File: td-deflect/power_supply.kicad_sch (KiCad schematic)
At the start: 94 parts, among them J13 Conn_01x02_Male, J14 Conn_01x02_Male, J18 Conn_01x02_Male, J2 Conn_01x02_Male, J9 Conn_01x02_Male, Q12 G3R450MT17J, Q13 BSZ42DN25NS3GATMA1, U13 MCP1416, U14 LT3758AEMSE

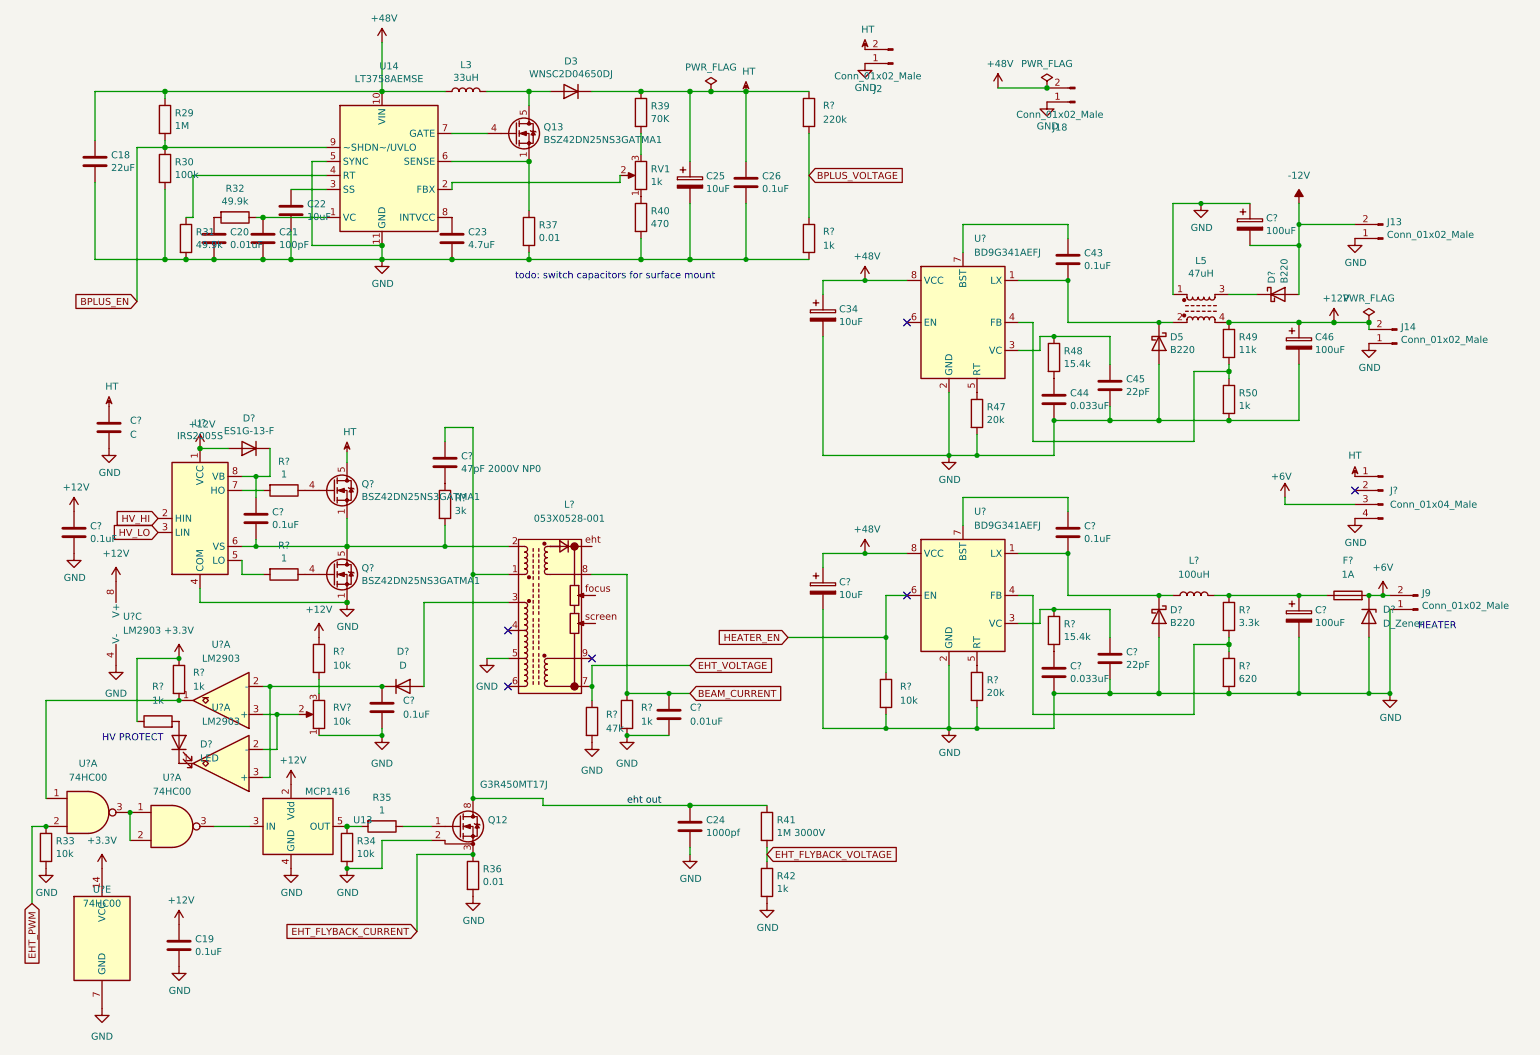
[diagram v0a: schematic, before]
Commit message: update kicad format and move flyback to separate sheet
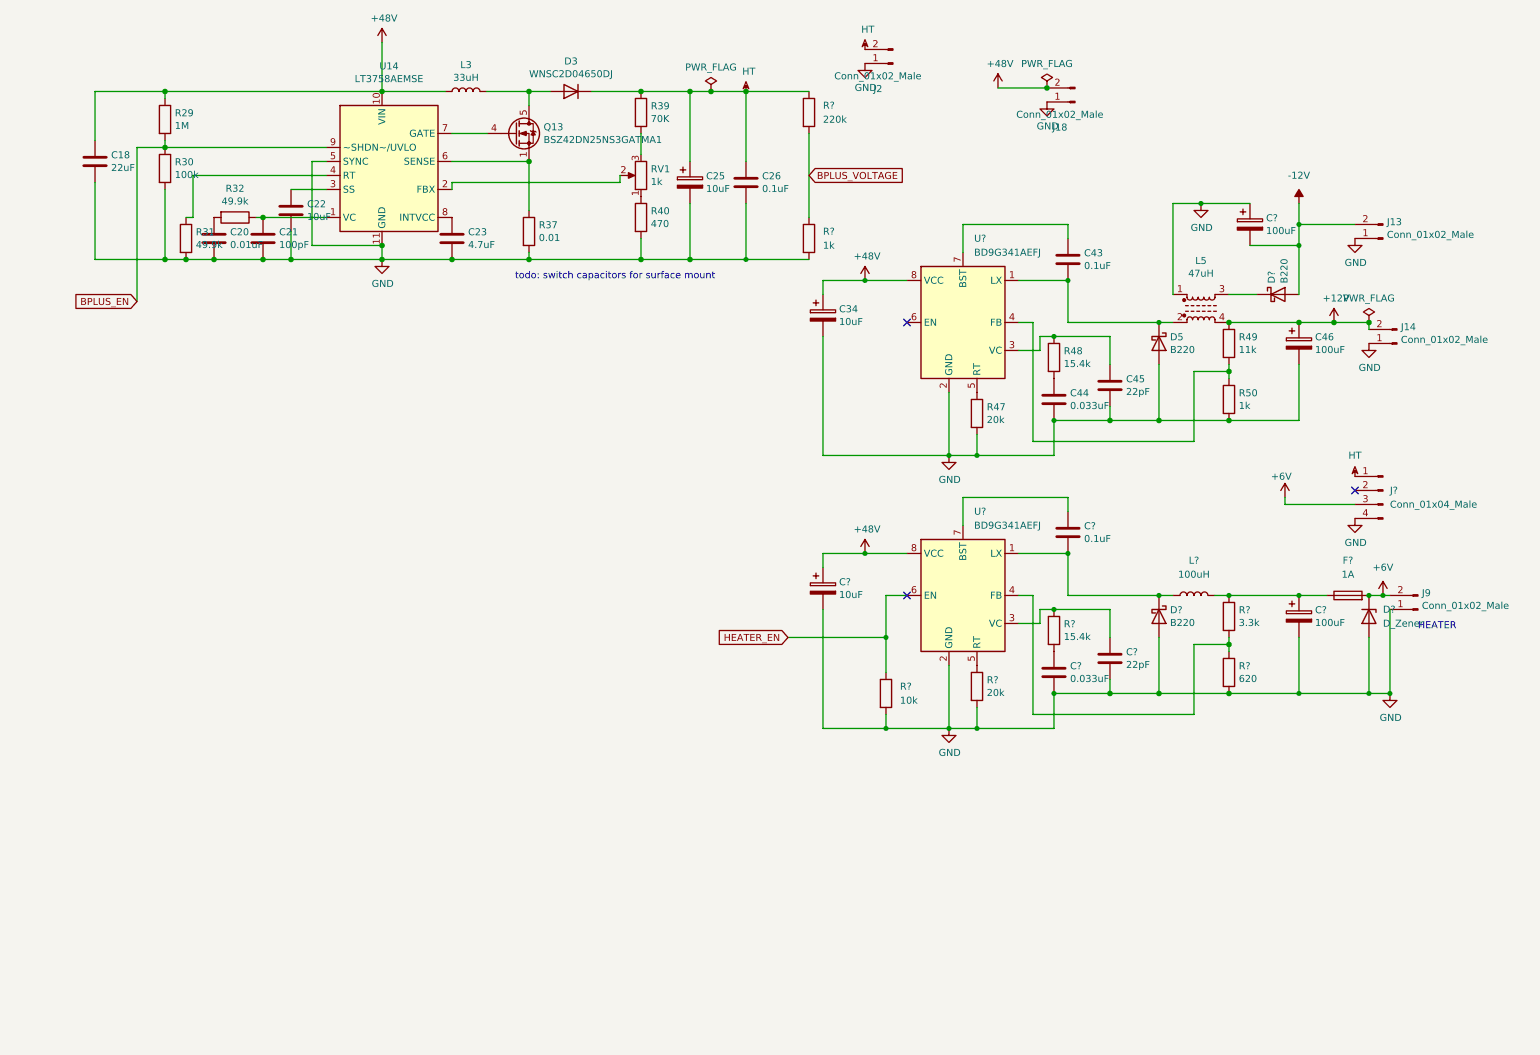
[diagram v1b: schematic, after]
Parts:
- removed C19, C? (x2): 0.1uF, Capacitor_SMD:C_0805_2012Metric_Pad1.15x1.40mm_HandSolder, symbol Device:C
- removed C24: 1000pf, Capacitor_THT:C_Rect_L18.0mm_W6.0mm_P15.00mm_FKS3_FKP3, symbol Device:C
- removed C?: C, symbol Device:C
- removed C?: 0.1uF, symbol Device:C
- removed C?: 47pF 2000V NP0, Capacitor_SMD:C_1206_3216Metric, symbol Device:C
- removed C?: 0.01uF, symbol Device:C
- removed D?: D, symbol Device:D
- removed D?: LED, symbol Device:LED
- removed D?: ES1G-13-F, Diode_SMD:D_SMA, symbol Diode:BA157
- removed L?: 053X0528-001, symbol td-hv:053X0528-001
- removed Q12: G3R450MT17J, Package_TO_SOT_SMD:TO-263-7_TabPin8, symbol Transistor_FET:C3M0280090J
- removed Q? (x2): BSZ42DN25NS3GATMA1, Package_TO_SOT_SMD:TDSON-8-1, symbol Transistor_FET:BSC082N10LSG
- removed R33, R34: 10k, Resistor_SMD:R_0805_2012Metric_Pad1.15x1.40mm_HandSolder, symbol Device:R
- removed R35, R? (x2): 1, Resistor_SMD:R_0805_2012Metric_Pad1.15x1.40mm_HandSolder, symbol Device:R
- removed R36: 0.01, Resistor_SMD:R_0805_2012Metric_Pad1.15x1.40mm_HandSolder, symbol Device:R
- removed R41: 1M 3000V, Resistor_SMD:R_2512_6332Metric, symbol Device:R
- removed R42: 1k, Resistor_SMD:R_0805_2012Metric_Pad1.15x1.40mm_HandSolder, symbol Device:R
- removed R? (x3): 1k, symbol Device:R
- removed R?: 3k, Resistor_SMD:R_2512_6332Metric, symbol Device:R
- removed R?: 10k, symbol Device:R
- removed R?: 47k, symbol Device:R
- removed RV?: 10k, symbol Device:R_Potentiometer
- removed U13: MCP1416, Package_TO_SOT_SMD:SOT-23-5, symbol Driver_FET:MCP1416
- removed U? (x3): 74HC00, symbol 74xx:74HC00
- removed U?: IRS2005S, Package_SO:SOIC-8_3.9x4.9mm_P1.27mm, symbol Driver_FET:IRS2005S
- removed U? (x3): LM2903, symbol Comparator:LM2903
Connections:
- no-connect marks 6 -> 3
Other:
- note removed: "HV PROTECT"

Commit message: Add independent cathode supply
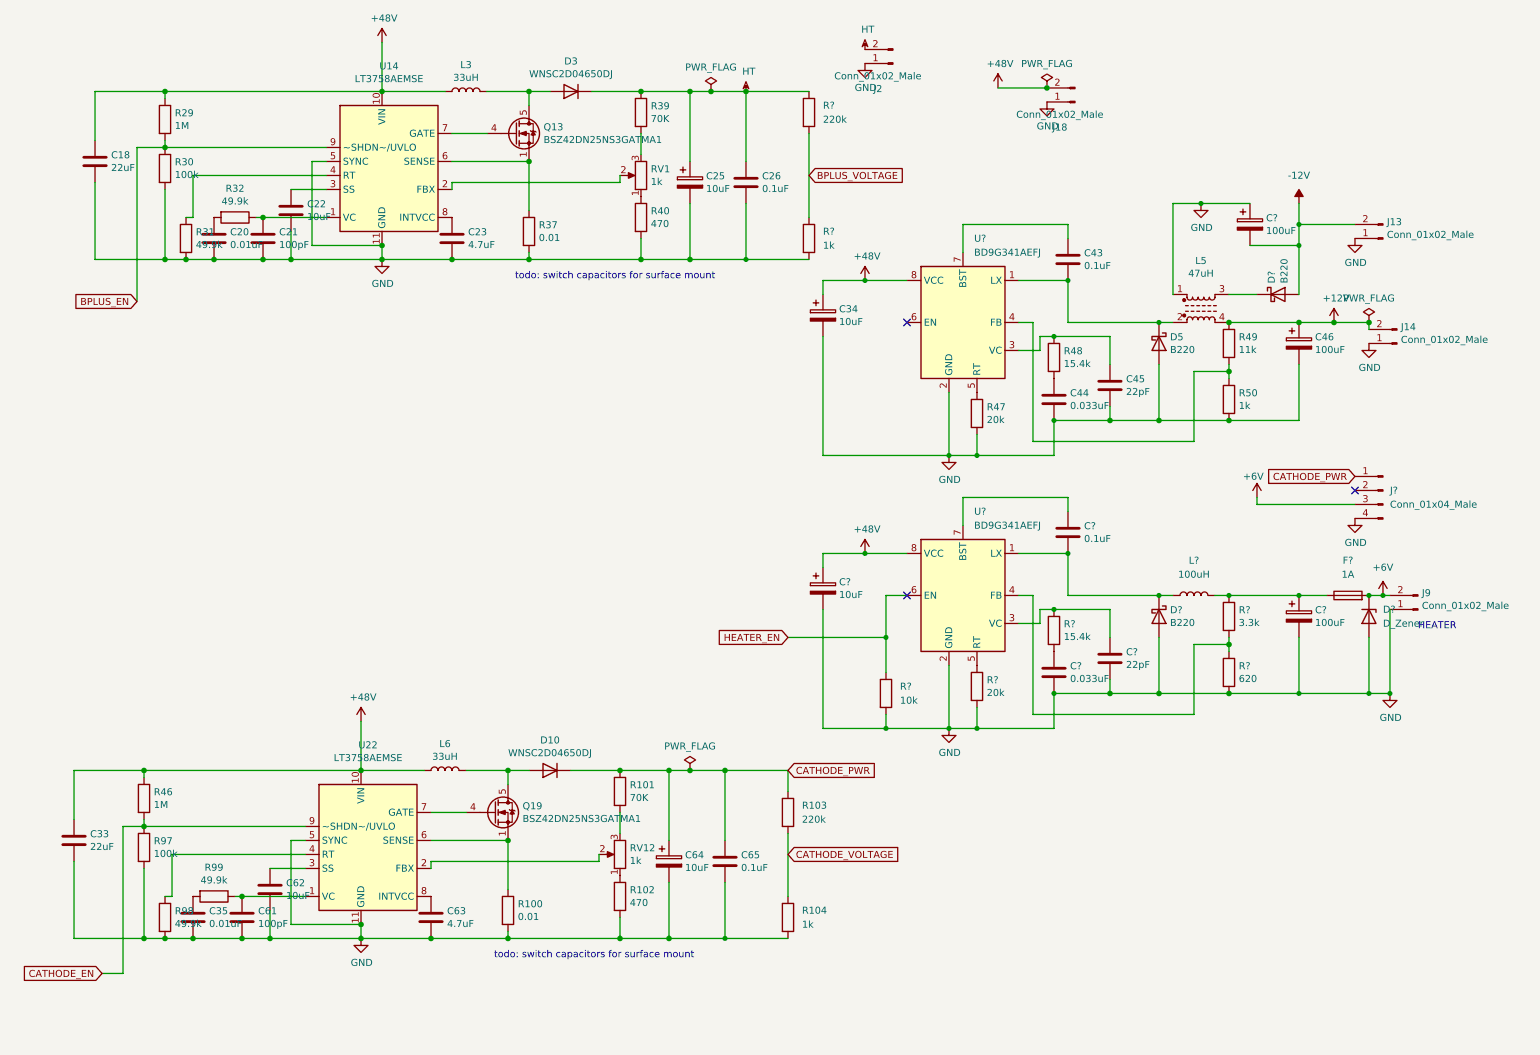
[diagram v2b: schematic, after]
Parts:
- added C33: 22uF, Capacitor_THT:CP_Radial_D8.0mm_P3.50mm, symbol Device:C
- added C35: 0.01uF, Capacitor_SMD:C_0805_2012Metric_Pad1.15x1.40mm_HandSolder, symbol Device:C
- added C61: 100pF, Capacitor_SMD:C_0805_2012Metric_Pad1.15x1.40mm_HandSolder, symbol Device:C
- added C62: 10uF, Capacitor_SMD:C_1206_3216Metric_Pad1.42x1.75mm_HandSolder, symbol Device:C
- added C63: 4.7uF, Capacitor_SMD:C_0805_2012Metric_Pad1.15x1.40mm_HandSolder, symbol Device:C
- added C64: 10uF, Capacitor_THT:CP_Radial_D8.0mm_P3.50mm, symbol Device:CP
- added C65: 0.1uF, Capacitor_SMD:C_1206_3216Metric_Pad1.42x1.75mm_HandSolder, symbol Device:C
- added D10: WNSC2D04650DJ, Package_TO_SOT_SMD:TO-252-2_TabPin1, symbol Diode:1N5402
- added L6: 33uH, Inductor_SMD:L_Bourns_SRR1260, symbol Device:L
- added Q19: BSZ42DN25NS3GATMA1, Package_TO_SOT_SMD:TDSON-8-1, symbol Transistor_FET:BSC082N10LSG
- added R100: 0.01, Resistor_SMD:R_0805_2012Metric_Pad1.15x1.40mm_HandSolder, symbol Device:R
- added R101: 70K, Resistor_SMD:R_1206_3216Metric_Pad1.42x1.75mm_HandSolder, symbol Device:R
- added R102: 470, Resistor_SMD:R_0805_2012Metric_Pad1.15x1.40mm_HandSolder, symbol Device:R
- added R103: 220k, symbol Device:R
- added R104: 1k, symbol Device:R
- added R46: 1M, Resistor_SMD:R_0805_2012Metric_Pad1.15x1.40mm_HandSolder, symbol Device:R
- added R97: 100k, Resistor_SMD:R_0805_2012Metric_Pad1.15x1.40mm_HandSolder, symbol Device:R
- added R98, R99: 49.9k, Resistor_SMD:R_0805_2012Metric_Pad1.15x1.40mm_HandSolder, symbol Device:R
- added RV12: 1k, Potentiometer_THT:Potentiometer_Bourns_3386P_Vertical, symbol Device:R_POT
- added U22: LT3758AEMSE, Package_SO:MSOP-10-1EP_3x3mm_P0.5mm_EP1.68x1.88mm, symbol Regulator_Switching:LT3757AEMSE
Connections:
- net +48V: now also C33.1, L6.1, R46.1, U22.10 (VIN)
- net GND: now also C33.2, C35.2, C61.2, C62.2, C63.2, C64.2, C65.2, R100.2, R102.2, R104.2, R97.2, R98.2, U22.11 (GND), U22.5 (SYNC)
- net HT: no longer J?.1 (Pin_1)
- new net: C61.1, R99.1, U22.1 (VC)
- new net: RV12.2, U22.2 (FBX)
- new net: C62.1, U22.3 (SS)
- new net: R98.1, U22.4 (RT)
- new net: Q19.1 (S), Q19.2 (S), Q19.3 (S), R100.1, U22.6 (SENSE)
- new net: Q19.4 (G), U22.7 (GATE)
- new net: C63.1, U22.8 (INTVCC)
- new net: C35.1, R99.2
- new net: R102.1, RV12.1
- new net: R101.2, RV12.3
- new net: D10.2 (A), L6.2, Q19.5 (D)
- new net CATHODE_EN: R46.2, R97.1, U22.9 (~SHDN~/UVLO)
- new net CATHODE_PWR: C64.1, C65.1, D10.1 (K), J?.1 (Pin_1), R101.1, R103.1
- new net CATHODE_VOLTAGE: R103.2, R104.1

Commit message: more updates
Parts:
- R103, R104: footprint (none) -> Resistor_SMD:R_0805_2012Metric_Pad1.15x1.40mm_HandSolder
- R73, R74, R75: renamed from R?; footprint (none) -> Resistor_SMD:R_0805_2012Metric_Pad1.15x1.40mm_HandSolder
- gave numbers to parts that had none: 18

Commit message: even more updates
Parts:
- F3: footprint (none) -> Fuse:Fuse_Schurter_UMT250
- J3: footprint (none) -> Connector_JST:JST_XH_B4B-XH-A_1x04_P2.50mm_Vertical
- L10: footprint (none) -> Inductor_SMD:L_Bourns_SRR1260
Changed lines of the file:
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@@
       (effects (font (size 1.27 1.27)))
     )
-    (property "Footprint" "" (at 224.79 120.65 0)
+    (property "Footprint" "Inductor_SMD:L_Bourns_SRR1260" (at 224.79 120.65 0)
       (effects (font (size 1.27 1.27)) hide)
     )
@@
       (effects (font (size 1.27 1.27)) (justify right))
     )
-    (property "Footprint" "" (at 259.08 101.6 0)
+    (property "Footprint" "Connector_JST:JST_XH_B4B-XH-A_1x04_P2.50mm_Vertical" (at 259.08 101.6 0)
       (effects (font (size 1.27 1.27)) hide)
     )
@@
       (effects (font (size 1.27 1.27)))
     )
-    (property "Footprint" "" (at 252.73 122.428 90)
-      (effects (font (size 1.27 1.27)) hide)
-    )
+    (property "Footprint" "Fuse:Fuse_Schurter_UMT250" (at 252.73 122.428 90)
+      (effects (font (size 1.27 1.27)) hide)
+    )

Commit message: small bugfix
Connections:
- no-connect marks 3 -> 2
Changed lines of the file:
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@@
   )
   (no_connect (at 254 101.6))
-  (no_connect (at 172.72 120.65))
   (no_connect (at 172.72 71.12))
   (wire (pts (xy 243.84 66.04) (xy 243.84 57.15))

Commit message: switch to new 0805 footprint
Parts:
- C20, C21, C23, C35, C43, C44, C45, C61, C63, C71, C72, C73: footprint Capacitor_SMD:C_0805_2012Metric_Pad1.15x1.40mm_HandSolder -> Capacitor_SMD:C_0805_2012Metric_Pad1.18x1.45mm_HandSolder
- C22, C26, C62, C65: footprint Capacitor_SMD:C_1206_3216Metric_Pad1.42x1.75mm_HandSolder -> Capacitor_SMD:C_1206_3216Metric_Pad1.33x1.80mm_HandSolder
- D17: footprint (none) -> Diode_SMD:D_0805_2012Metric_Pad1.15x1.40mm_HandSolder
- R100, R102, R103, R104, R29, R30, R31, R32, R37, R40, R46, R47, R48, R49, R50, R73, R74, R75, R76, R77, R78, R79, R97, R98, R99: footprint Resistor_SMD:R_0805_2012Metric_Pad1.15x1.40mm_HandSolder -> Resistor_SMD:R_0805_2012Metric_Pad1.20x1.40mm_HandSolder
- R101, R39: footprint Resistor_SMD:R_1206_3216Metric_Pad1.42x1.75mm_HandSolder -> Resistor_SMD:R_1206_3216Metric_Pad1.30x1.75mm_HandSolder
